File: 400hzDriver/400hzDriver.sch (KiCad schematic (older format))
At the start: 91 parts

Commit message: Updated resistor values for FET turn off transistors. Updated PWM max dutycycle in firmware.
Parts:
- R? (x4): value 10 -> 5
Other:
- moved on the sheet: C?, D?, J?, R?
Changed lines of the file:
@@
 L Device:C C?
 U 1 1 5FBE8317
-P 6350 2700
-F 0 "C?" H 6465 2746 50  0000 L CNN
-F 1 "C" H 6465 2655 50  0000 L CNN
-F 2 "" H 6388 2550 50  0001 C CNN
-F 3 "~" H 6350 2700 50  0001 C CNN
-	1    6350 2700
+P 6850 3250
+F 0 "C?" H 6965 3296 50  0000 L CNN
+F 1 "C" H 6965 3205 50  0000 L CNN
+F 2 "" H 6888 3100 50  0001 C CNN
+F 3 "~" H 6850 3250 50  0001 C CNN
+	1    6850 3250
 	1    0    0    -1
 $EndComp
@@
 L Device:C C?
 U 1 1 5FBE8FE8
-P 6650 2700
-F 0 "C?" H 6765 2746 50  0000 L CNN
-F 1 "C" H 6765 2655 50  0000 L CNN
-F 2 "" H 6688 2550 50  0001 C CNN
-F 3 "~" H 6650 2700 50  0001 C CNN
-	1    6650 2700
+P 7150 3250
+F 0 "C?" H 7265 3296 50  0000 L CNN
+F 1 "C" H 7265 3205 50  0000 L CNN
+F 2 "" H 7188 3100 50  0001 C CNN
+F 3 "~" H 7150 3250 50  0001 C CNN
+	1    7150 3250
 	1    0    0    -1
 $EndComp
@@
 L Device:C C?
 U 1 1 5FBE917E
-P 6950 2700
-F 0 "C?" H 7065 2746 50  0000 L CNN
-F 1 "C" H 7065 2655 50  0000 L CNN
-F 2 "" H 6988 2550 50  0001 C CNN
-F 3 "~" H 6950 2700 50  0001 C CNN
-	1    6950 2700
+P 7450 3250
+F 0 "C?" H 7565 3296 50  0000 L CNN
+F 1 "C" H 7565 3205 50  0000 L CNN
+F 2 "" H 7488 3100 50  0001 C CNN
+F 3 "~" H 7450 3250 50  0001 C CNN
+	1    7450 3250
 	1    0    0    -1
 $EndComp
@@
 L Device:C C?
 U 1 1 5FBE94D3
-P 7250 2700
-F 0 "C?" H 7365 2746 50  0000 L CNN
-F 1 "C" H 7365 2655 50  0000 L CNN
-F 2 "" H 7288 2550 50  0001 C CNN
-F 3 "~" H 7250 2700 50  0001 C CNN
-	1    7250 2700
-	1    0    0    -1
-$EndComp
-Wire Wire Line
-	6350 2850 6650 2850
-Wire Wire Line
-	6650 2850 6950 2850
-Connection ~ 6650 2850
-Wire Wire Line
-	7250 2850 6950 2850
-Connection ~ 6950 2850
-Wire Wire Line
-	7250 2550 6950 2550
-Wire Wire Line
-	6650 2550 6950 2550
-Connection ~ 6950 2550
-Wire Wire Line
-	6350 2550 6650 2550
-Connection ~ 6650 2550
+P 7750 3250
+F 0 "C?" H 7865 3296 50  0000 L CNN
+F 1 "C" H 7865 3205 50  0000 L CNN
+F 2 "" H 7788 3100 50  0001 C CNN
+F 3 "~" H 7750 3250 50  0001 C CNN
+	1    7750 3250
+	1    0    0    -1
+$EndComp
+Wire Wire Line
+	6850 3400 7150 3400
+Wire Wire Line
+	7150 3400 7450 3400
+Connection ~ 7150 3400
+Wire Wire Line
+	7750 3400 7450 3400
+Connection ~ 7450 3400
+Wire Wire Line
+	7750 3100 7450 3100
+Wire Wire Line
+	7150 3100 7450 3100
+Connection ~ 7450 3100
+Wire Wire Line
+	6850 3100 7150 3100
+Connection ~ 7150 3100
 $Comp
 L power:GND #PWR?
 U 1 1 5FBE9EB7
-P 6650 2900
-F 0 "#PWR?" H 6650 2650 50  0001 C CNN
-F 1 "GND" H 6655 2727 50  0000 C CNN
-F 2 "" H 6650 2900 50  0001 C CNN
-F 3 "" H 6650 2900 50  0001 C CNN
-	1    6650 2900
-	1    0    0    -1
-$EndComp
-Wire Wire Line
-	6650 2850 6650 2900
+P 7150 3450
+F 0 "#PWR?" H 7150 3200 50  0001 C CNN
+F 1 "GND" H 7155 3277 50  0000 C CNN
+F 2 "" H 7150 3450 50  0001 C CNN
+F 3 "" H 7150 3450 50  0001 C CNN
+	1    7150 3450
+	1    0    0    -1
+$EndComp
+Wire Wire Line
+	7150 3400 7150 3450
 $Comp
 L power:GND #PWR?
@@
 L power:+5V #PWR?
 U 1 1 5FBF96D8
-P 6650 2550
-F 0 "#PWR?" H 6650 2400 50  0001 C CNN
-F 1 "+5V" H 6665 2723 50  0000 C CNN
-F 2 "" H 6650 2550 50  0001 C CNN
-F 3 "" H 6650 2550 50  0001 C CNN
-	1    6650 2550
+P 7150 3100
+F 0 "#PWR?" H 7150 2950 50  0001 C CNN
+F 1 "+5V" H 7165 3273 50  0000 C CNN
+F 2 "" H 7150 3100 50  0001 C CNN
+F 3 "" H 7150 3100 50  0001 C CNN
+	1    7150 3100
 	1    0    0    -1
 $EndComp
@@
 	0    -1   1    0
 $EndComp
-$Comp
-L power:GND #PWR?
-U 1 1 5FC8611F
-P 150 3400
-F 0 "#PWR?" H 150 3150 50  0001 C CNN
-F 1 "GND" H 155 3227 50  0000 C CNN
-F 2 "" H 150 3400 50  0001 C CNN
-F 3 "" H 150 3400 50  0001 C CNN
-	1    150  3400
-	1    0    0    -1
-$EndComp
 Wire Wire Line
 	1700 4000 1900 4000
@@
 L Connector_Generic:Conn_01x05 J?
 U 1 1 5FD3D0B1
-P 9500 1700
-F 0 "J?" H 9580 1742 50  0000 L CNN
-F 1 "ICSP" H 9580 1651 50  0000 L CNN
-F 2 "" H 9500 1700 50  0001 C CNN
-F 3 "~" H 9500 1700 50  0001 C CNN
-	1    9500 1700
+P 10700 3000
+F 0 "J?" H 10780 3042 50  0000 L CNN
+F 1 "ICSP" H 10780 2951 50  0000 L CNN
+F 2 "" H 10700 3000 50  0001 C CNN
+F 3 "~" H 10700 3000 50  0001 C CNN
+	1    10700 3000
 	1    0    0    -1
 $EndComp
@@
 L Device:D D?
 U 1 1 5FD3DF1E
-P 8450 1900
-F 0 "D?" V 8496 1821 50  0000 R CNN
-F 1 "D" V 8405 1821 50  0000 R CNN
-F 2 "" H 8450 1900 50  0001 C CNN
-F 3 "~" H 8450 1900 50  0001 C CNN
-	1    8450 1900
+P 9650 3200
+F 0 "D?" V 9696 3121 50  0000 R CNN
+F 1 "D" V 9605 3121 50  0000 R CNN
+F 2 "" H 9650 3200 50  0001 C CNN
+F 3 "~" H 9650 3200 50  0001 C CNN
+	1    9650 3200
 	0    -1   -1   0
 $EndComp
@@
 L Device:R R?
 U 1 1 5FD3E527
-P 8450 1600
-F 0 "R?" H 8380 1554 50  0000 R CNN
-F 1 "2K" H 8380 1645 50  0000 R CNN
-F 2 "" V 8380 1600 50  0001 C CNN
-F 3 "~" H 8450 1600 50  0001 C CNN
-	1    8450 1600
+P 9650 2900
+F 0 "R?" H 9580 2854 50  0000 R CNN
+F 1 "2K" H 9580 2945 50  0000 R CNN
+F 2 "" V 9580 2900 50  0001 C CNN
+F 3 "~" H 9650 2900 50  0001 C CNN
+	1    9650 2900
 	-1   0    0    1
 $EndComp
@@
 L power:GND #PWR?
 U 1 1 5FD3F2C1
-P 9100 2050
-F 0 "#PWR?" H 9100 1800 50  0001 C CNN
-F 1 "GND" H 9105 1877 50  0000 C CNN
-F 2 "" H 9100 2050 50  0001 C CNN
-F 3 "" H 9100 2050 50  0001 C CNN
-	1    9100 2050
-	1    0    0    -1
-$EndComp
-Wire Wire Line
-	9300 1700 9100 1700
-Wire Wire Line
-	9100 1700 9100 2050
-Wire Wire Line
-	9300 1800 8950 1800
-Wire Wire Line
-	8950 1800 8950 1700
+P 10300 3350
+F 0 "#PWR?" H 10300 3100 50  0001 C CNN
+F 1 "GND" H 10305 3177 50  0000 C CNN
+F 2 "" H 10300 3350 50  0001 C CNN
+F 3 "" H 10300 3350 50  0001 C CNN
+	1    10300 3350
+	1    0    0    -1
+$EndComp
+Wire Wire Line
+	10500 3000 10300 3000
+Wire Wire Line
+	10300 3000 10300 3350
+Wire Wire Line
+	10500 3100 10150 3100
+Wire Wire Line
+	10150 3100 10150 3000
 $Comp
 L power:+5V #PWR?
 U 1 1 5FD50290
-P 8950 1700
-F 0 "#PWR?" H 8950 1550 50  0001 C CNN
-F 1 "+5V" H 8965 1873 50  0000 C CNN
-F 2 "" H 8950 1700 50  0001 C CNN
-F 3 "" H 8950 1700 50  0001 C CNN
-	1    8950 1700
-	1    0    0    -1
-$EndComp
-Text Label 9300 1500 2    50   ~ 0
+P 10150 3000
+F 0 "#PWR?" H 10150 2850 50  0001 C CNN
+F 1 "+5V" H 10165 3173 50  0000 C CNN
+F 2 "" H 10150 3000 50  0001 C CNN
+F 3 "" H 10150 3000 50  0001 C CNN
+	1    10150 3000
+	1    0    0    -1
+$EndComp
+Text Label 10500 2800 2    50   ~ 0
 PGMC
-Text Label 9300 1600 2    50   ~ 0
+Text Label 10500 2900 2    50   ~ 0
 PGMD
 Text Label 10250 3750 0    50   ~ 0
@@
 L power:+5V #PWR?
 U 1 1 5FD5286D
-P 8450 1450
-F 0 "#PWR?" H 8450 1300 50  0001 C CNN
-F 1 "+5V" H 8465 1623 50  0000 C CNN
-F 2 "" H 8450 1450 50  0001 C CNN
-F 3 "" H 8450 1450 50  0001 C CNN
-	1    8450 1450
-	1    0    0    -1
-$EndComp
-Text Label 8450 2050 2    50   ~ 0
+P 9650 2750
+F 0 "#PWR?" H 9650 2600 50  0001 C CNN
+F 1 "+5V" H 9665 2923 50  0000 C CNN
+F 2 "" H 9650 2750 50  0001 C CNN
+F 3 "" H 9650 2750 50  0001 C CNN
+	1    9650 2750
+	1    0    0    -1
+$EndComp
+Text Label 9650 3350 2    50   ~ 0
 MCLR
 Wire Wire Line
-	9300 1900 8750 1900
-Wire Wire Line
-	8750 1900 8750 2050
-Wire Wire Line
-	8750 2050 8450 2050
+	10500 3200 9950 3200
+Wire Wire Line
+	9950 3200 9950 3350
+Wire Wire Line
+	9950 3350 9650 3350
 Text Label 6450 5050 2    50   ~ 0
 MCLR
@@
 	600  650  3400 650
 Wire Notes Line
-	3400 650  3400 2100
-Wire Notes Line
-	3400 2100 4900 2100
-Wire Notes Line
 	4900 2100 4900 5400
 $Comp
@@
 P 2150 3550
 F 0 "R?" V 1943 3550 50  0000 C CNN
-F 1 "10" V 2034 3550 50  0000 C CNN
+F 1 "5" V 2034 3550 50  0000 C CNN
 F 2 "" V 2080 3550 50  0001 C CNN
 F 3 "~" H 2150 3550 50  0001 C CNN
@@
 P 1500 3450
 F 0 "R?" V 1293 3450 50  0000 C CNN
-F 1 "10" V 1384 3450 50  0000 C CNN
+F 1 "5" V 1384 3450 50  0000 C CNN
 F 2 "" V 1430 3450 50  0001 C CNN
 F 3 "~" H 1500 3450 50  0001 C CNN
@@
 P 2150 5400
 F 0 "R?" V 1943 5400 50  0000 C CNN
-F 1 "10" V 2034 5400 50  0000 C CNN
+F 1 "5" V 2034 5400 50  0000 C CNN
 F 2 "" V 2080 5400 50  0001 C CNN
 F 3 "~" H 2150 5400 50  0001 C CNN
@@
 P 1500 5500
 F 0 "R?" V 1293 5500 50  0000 C CNN
-F 1 "10" V 1384 5500 50  0000 C CNN
+F 1 "5" V 1384 5500 50  0000 C CNN
 F 2 "" V 1430 5500 50  0001 C CNN
 F 3 "~" H 1500 5500 50  0001 C CNN

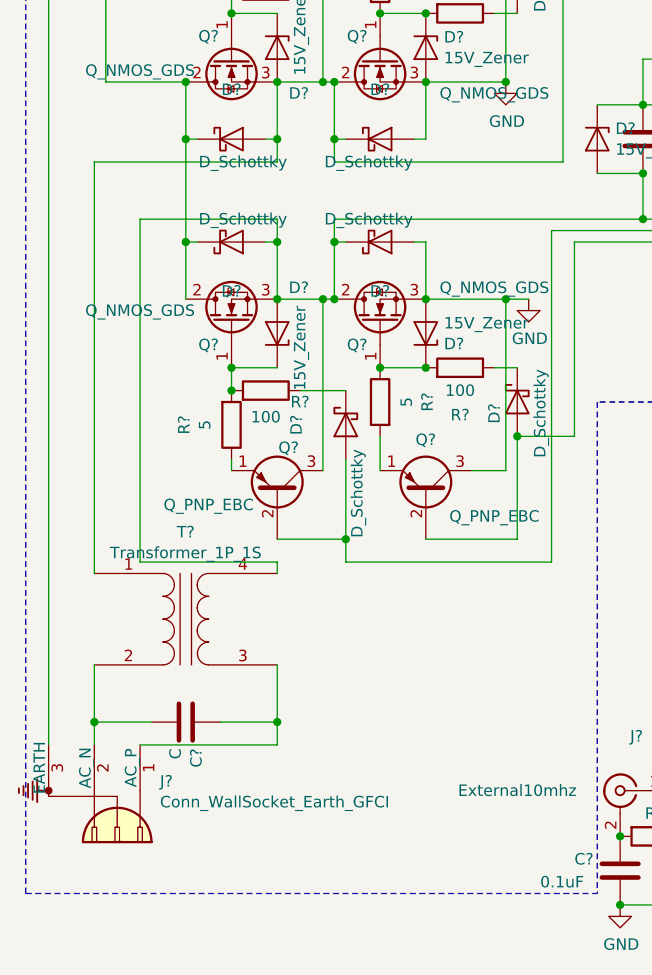
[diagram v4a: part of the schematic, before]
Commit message: Updated Output Filtering.
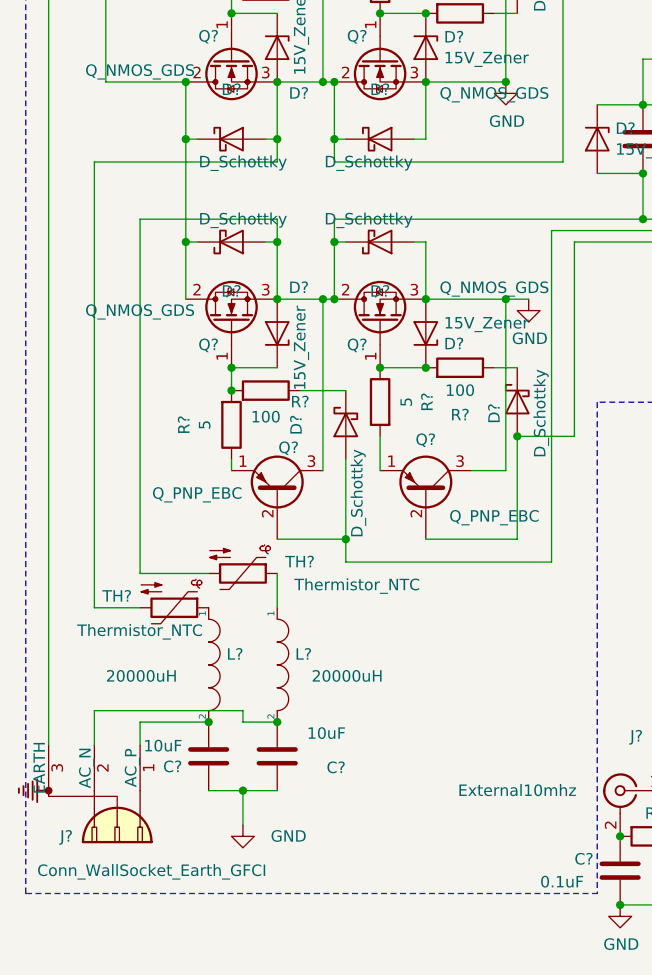
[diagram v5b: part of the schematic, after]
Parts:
- removed T?: Transformer_1P_1S, symbol Device:Transformer_1P_1S
- added C?: 10uF, symbol Device:C
- added L? (x2): 20000uH, symbol pspice:INDUCTOR
- added TH? (x2): Thermistor_NTC, symbol Device:Thermistor_NTC
- C?: value C -> 10uF
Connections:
- net GND: now also C?.1, C?.1
- net at C?.2, D?.1 (K), D?.2 (A)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: now also TH?.2 (x2)
- net at C?.2, J?.2 (AC_N): now also L?.2
- net at J?.1 (AC_P): now also C?.2, L?.2; no longer C?.1
- new net: L?.1, TH?.1 (x2)
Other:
- moved on the sheet: C?
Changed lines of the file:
@@
 	1400 1250 2700 1250
-$Comp
-L Device:Transformer_1P_1S T?
-U 1 1 5FCF490A
-P 1300 6350
-F 0 "T?" H 1300 6731 50  0000 C CNN
-F 1 "Transformer_1P_1S" H 1300 6640 50  0000 C CNN
-F 2 "" H 1300 6350 50  0001 C CNN
-F 3 "~" H 1300 6350 50  0001 C CNN
-	1    1300 6350
-	1    0    0    -1
-$EndComp
 $Comp
 L Device:C C?
 U 1 1 5FCF5035
-P 1300 6800
-F 0 "C?" H 1415 6846 50  0000 L CNN
-F 1 "C" H 1415 6755 50  0000 L CNN
-F 2 "" H 1338 6650 50  0001 C CNN
-F 3 "~" H 1300 6800 50  0001 C CNN
-	1    1300 6800
-	0    1    1    0
+P 1700 6950
+F 0 "C?" H 1400 7000 50  0000 L CNN
+F 1 "10uF" H 1400 6850 50  0000 L CNN
+F 2 "" H 1738 6800 50  0001 C CNN
+F 3 "~" H 1700 6950 50  0001 C CNN
+	1    1700 6950
+	-1   0    0    1
 $EndComp
 Wire Wire Line
 	1950 4350 1950 4250
-Wire Wire Line
-	1700 6550 1700 6800
-Wire Wire Line
-	1700 6800 1450 6800
-Wire Wire Line
-	900  6550 900  6800
-Wire Wire Line
-	900  6800 1150 6800
 $Comp
 L Device:R R?
@@
 U 1 1 5FD22F7C
 P 900 7100
-F 0 "J?" V 859 7387 50  0000 L CNN
-F 1 "Conn_WallSocket_Earth_GFCI" V 950 7387 50  0000 L CNN
+F 0 "J?" V 1100 6950 50  0000 L CNN
+F 1 "Conn_WallSocket_Earth_GFCI" V 1250 6850 50  0000 L CNN
 F 2 "" H 600 7200 50  0001 C CNN
 F 3 "~" H 600 7200 50  0001 C CNN
@@
 P 1700 5800
 F 0 "Q?" V 1900 5850 50  0000 C CNN
-F 1 "Q_PNP_EBC" V 1650 5500 50  0000 C CNN
+F 1 "Q_PNP_EBC" V 1700 5450 50  0000 C CNN
 F 2 "" H 1900 5900 50  0001 C CNN
 F 3 "~" H 1700 5800 50  0001 C CNN
@@
 	700  1750 1400 1750
 Wire Wire Line
-	900  6800 900  6900
-Connection ~ 900  6800
-Wire Wire Line
-	1100 6900 1700 6900
-Wire Wire Line
-	1700 6900 1700 6800
-Connection ~ 1700 6800
-Wire Wire Line
-	1700 6150 1700 6100
-Wire Wire Line
-	1700 6100 1100 6100
-Wire Wire Line
-	1100 6100 1100 4600
-Wire Wire Line
 	1100 4600 1700 4600
 Wire Wire Line
 	1700 4600 1700 4700
 Connection ~ 1700 4700
-Wire Wire Line
-	900  6150 900  4350
 Wire Wire Line
 	900  4350 1700 4350
@@
 	3200 7600 4100 7600
 Connection ~ 3200 7600
+$Comp
+L pspice:INDUCTOR L?
+U 1 1 5FCA8C9E
+P 1400 6550
+F 0 "L?" V 1354 6628 50  0000 L CNN
+F 1 "20000uH" V 1450 6100 50  0000 L CNN
+F 2 "" H 1400 6550 50  0001 C CNN
+F 3 "~" H 1400 6550 50  0001 C CNN
+	1    1400 6550
+	0    1    1    0
+$EndComp
+$Comp
+L pspice:INDUCTOR L?
+U 1 1 5FCA959E
+P 1700 6550
+F 0 "L?" V 1654 6628 50  0000 L CNN
+F 1 "20000uH" V 1750 6700 50  0000 L CNN
+F 2 "" H 1700 6550 50  0001 C CNN
+F 3 "~" H 1700 6550 50  0001 C CNN
+	1    1700 6550
+	0    1    1    0
+$EndComp
+$Comp
+L Device:C C?
+U 1 1 5FCAAB14
+P 1400 6950
+F 0 "C?" H 1515 6996 50  0000 L CNN
+F 1 "10uF" H 1515 6905 50  0000 L CNN
+F 2 "" H 1438 6800 50  0001 C CNN
+F 3 "~" H 1400 6950 50  0001 C CNN
+	1    1400 6950
+	-1   0    0    1
+$EndComp
+$Comp
+L power:GND #PWR?
+U 1 1 5FCAADFA
+P 1550 7250
+F 0 "#PWR?" H 1550 7000 50  0001 C CNN
+F 1 "GND" H 1750 7200 50  0000 C CNN
+F 2 "" H 1550 7250 50  0001 C CNN
+F 3 "" H 1550 7250 50  0001 C CNN
+	1    1550 7250
+	1    0    0    -1
+$EndComp
+Wire Wire Line
+	1700 7100 1550 7100
+Wire Wire Line
+	1550 7250 1550 7100
+Connection ~ 1550 7100
+Wire Wire Line
+	1550 7100 1400 7100
+$Comp
+L Device:Thermistor_NTC TH?
+U 1 1 5FCE13D3
+P 1550 6150
+F 0 "TH?" V 1500 6400 50  0000 C CNN
+F 1 "Thermistor_NTC" V 1600 6650 50  0000 C CNN
+F 2 "" H 1550 6200 50  0001 C CNN
+F 3 "~" H 1550 6200 50  0001 C CNN
+	1    1550 6150
+	0    1    1    0
+$EndComp
+$Comp
+L Device:Thermistor_NTC TH?
+U 1 1 5FCE3485
+P 1250 6300
+F 0 "TH?" V 1200 6050 50  0000 C CNN
+F 1 "Thermistor_NTC" V 1350 6150 50  0000 C CNN
+F 2 "" H 1250 6350 50  0001 C CNN
+F 3 "~" H 1250 6350 50  0001 C CNN
+	1    1250 6300
+	0    1    1    0
+$EndComp
+Wire Wire Line
+	1700 6150 1700 6300
+Wire Wire Line
+	1400 6150 1100 6150
+Wire Wire Line
+	1100 6150 1100 4600
+Wire Wire Line
+	900  4350 900  6300
+Wire Wire Line
+	900  6300 1100 6300
+Wire Wire Line
+	1100 6900 1100 6800
+Wire Wire Line
+	1100 6800 1400 6800
+Connection ~ 1400 6800
+Wire Wire Line
+	900  6900 900  6750
+Wire Wire Line
+	900  6750 1550 6750
+Wire Wire Line
+	1550 6750 1550 6800
+Wire Wire Line
+	1550 6800 1700 6800
+Connection ~ 1700 6800
 $EndSCHEMATC

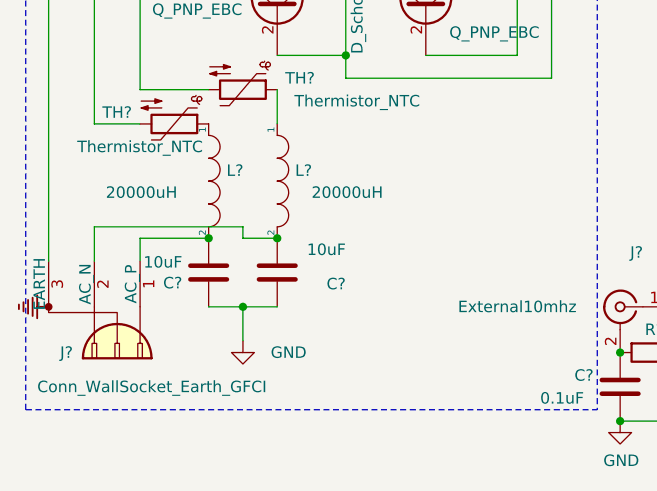
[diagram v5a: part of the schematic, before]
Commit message: Updated Output Filter. Seems to work well enough and doesn't draw too much idle current under simulation. Voltage may sag under higher loads however. Waiting for new parts to test in real life.
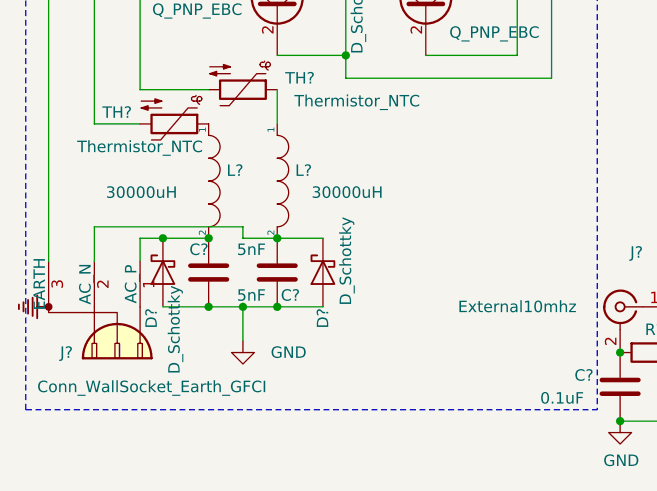
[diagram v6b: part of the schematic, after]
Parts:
- added D? (x2): D_Schottky, symbol Device:D_Schottky
- C? (x2): value 10uF -> 5nF
- L? (x2): value 20000uH -> 30000uH
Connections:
- net GND: now also D?.2 (A), D?.2 (A)
- net at C?.2, J?.1 (AC_P), L?.2: now also D?.1 (K)
- net at C?.2, J?.2 (AC_N), L?.2: now also D?.1 (K)
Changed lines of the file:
@@
 U 1 1 5FCF5035
 P 1700 6950
-F 0 "C?" H 1400 7000 50  0000 L CNN
-F 1 "10uF" H 1400 6850 50  0000 L CNN
+F 0 "C?" H 1600 7050 50  0000 L CNN
+F 1 "5nF" H 1750 6850 50  0000 L CNN
 F 2 "" H 1738 6800 50  0001 C CNN
 F 3 "~" H 1700 6950 50  0001 C CNN
@@
 P 1400 6550
 F 0 "L?" V 1354 6628 50  0000 L CNN
-F 1 "20000uH" V 1450 6100 50  0000 L CNN
+F 1 "30000uH" V 1450 6100 50  0000 L CNN
 F 2 "" H 1400 6550 50  0001 C CNN
 F 3 "~" H 1400 6550 50  0001 C CNN
@@
 P 1700 6550
 F 0 "L?" V 1654 6628 50  0000 L CNN
-F 1 "20000uH" V 1750 6700 50  0000 L CNN
+F 1 "30000uH" V 1750 6700 50  0000 L CNN
 F 2 "" H 1700 6550 50  0001 C CNN
 F 3 "~" H 1700 6550 50  0001 C CNN
@@
 U 1 1 5FCAAB14
 P 1400 6950
-F 0 "C?" H 1515 6996 50  0000 L CNN
-F 1 "10uF" H 1515 6905 50  0000 L CNN
+F 0 "C?" H 1400 6850 50  0000 L CNN
+F 1 "5nF" H 1150 7050 50  0000 L CNN
 F 2 "" H 1438 6800 50  0001 C CNN
 F 3 "~" H 1400 6950 50  0001 C CNN
@@
 	1550 7250 1550 7100
 Connection ~ 1550 7100
-Wire Wire Line
-	1550 7100 1400 7100
 $Comp
 L Device:Thermistor_NTC TH?
@@
 	1100 6900 1100 6800
 Wire Wire Line
-	1100 6800 1400 6800
+	1100 6800 1200 6800
 Connection ~ 1400 6800
 Wire Wire Line
@@
 	1550 6800 1700 6800
 Connection ~ 1700 6800
+$Comp
+L Device:D_Schottky D?
+U 1 1 5FCACBE9
+P 1900 6950
+F 0 "D?" H 2100 6950 50  0000 C CNN
+F 1 "D_Schottky" H 1850 6850 50  0000 C CNN
+F 2 "" H 1900 6950 50  0001 C CNN
+F 3 "~" H 1900 6950 50  0001 C CNN
+	1    1900 6950
+	0    -1   1    0
+$EndComp
+$Comp
+L Device:D_Schottky D?
+U 1 1 5FCAD578
+P 1200 6950
+F 0 "D?" H 1400 7000 50  0000 C CNN
+F 1 "D_Schottky" H 1450 6900 50  0000 C CNN
+F 2 "" H 1200 6950 50  0001 C CNN
+F 3 "~" H 1200 6950 50  0001 C CNN
+	1    1200 6950
+	0    -1   1    0
+$EndComp
+Connection ~ 1200 6800
+Wire Wire Line
+	1200 6800 1400 6800
+Wire Wire Line
+	1900 7100 1700 7100
+Connection ~ 1700 7100
+Wire Wire Line
+	1200 7100 1400 7100
+Connection ~ 1400 7100
+Wire Wire Line
+	1400 7100 1550 7100
+Wire Wire Line
+	1900 6800 1700 6800
 $EndSCHEMATC
